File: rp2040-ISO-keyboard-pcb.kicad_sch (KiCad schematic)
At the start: 32 parts

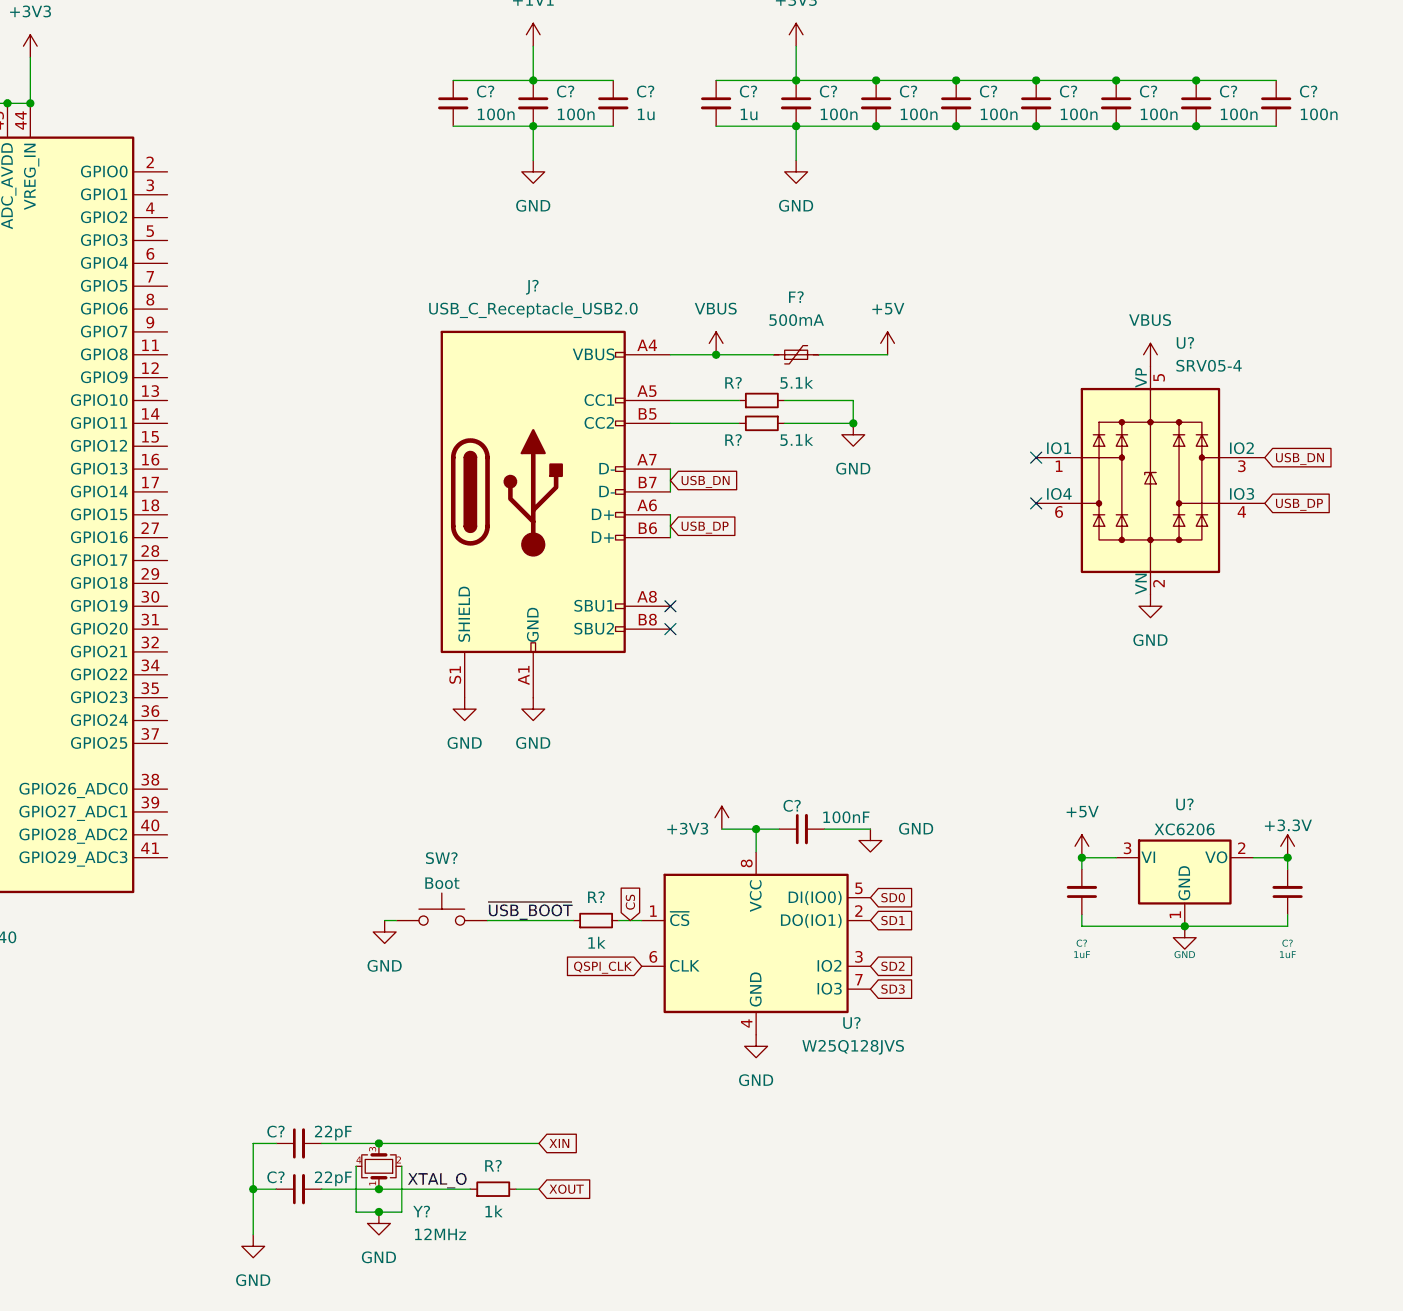
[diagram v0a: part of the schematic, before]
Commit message: added keymatrix with stabs
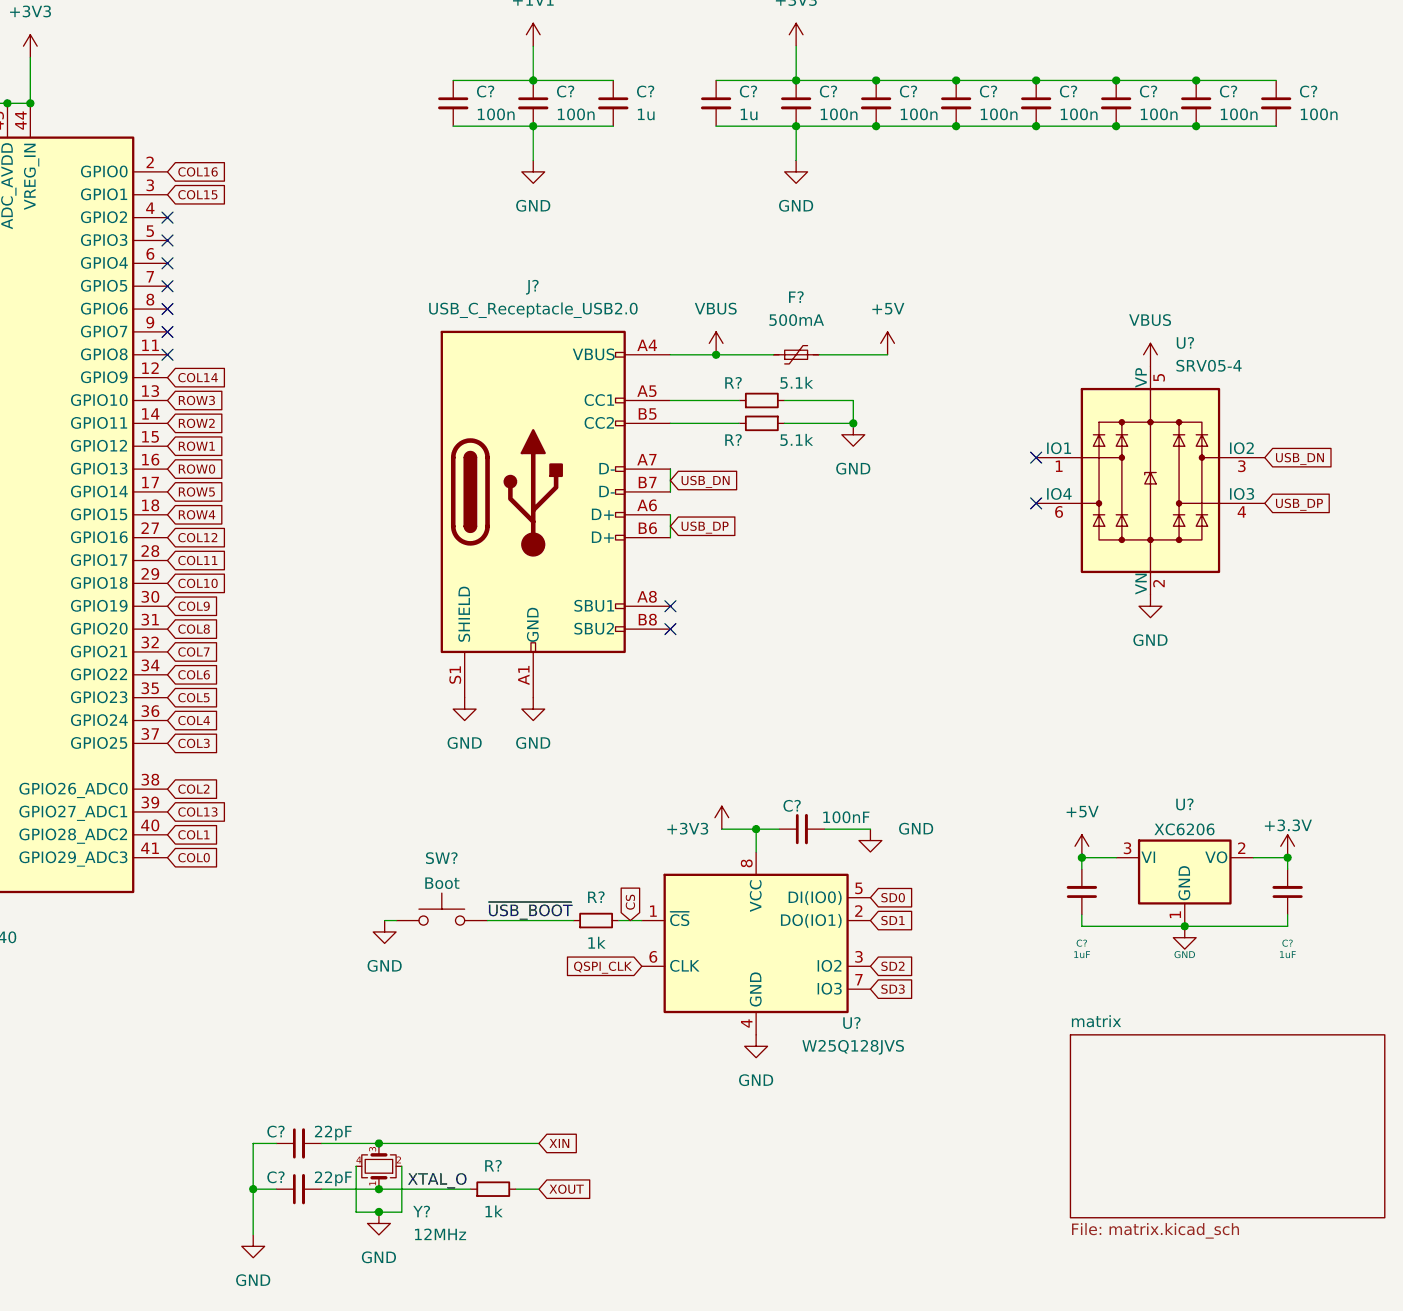
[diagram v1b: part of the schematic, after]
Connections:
- net COL14: now reaches U?.12 (GPIO9)
- net ROW3: now reaches U?.13 (GPIO10)
- net ROW2: now reaches U?.14 (GPIO11)
- net ROW1: now reaches U?.15 (GPIO12)
- net ROW0: now reaches U?.16 (GPIO13)
- net ROW5: now reaches U?.17 (GPIO14)
- net ROW4: now reaches U?.18 (GPIO15)
- net COL16: now reaches U?.2 (GPIO0)
- net COL12: now reaches U?.27 (GPIO16)
- net COL11: now reaches U?.28 (GPIO17)
- net COL10: now reaches U?.29 (GPIO18)
- net COL15: now reaches U?.3 (GPIO1)
- net COL9: now reaches U?.30 (GPIO19)
- net COL8: now reaches U?.31 (GPIO20)
- net COL7: now reaches U?.32 (GPIO21)
- net COL6: now reaches U?.34 (GPIO22)
- net COL5: now reaches U?.35 (GPIO23)
- net COL4: now reaches U?.36 (GPIO24)
- net COL3: now reaches U?.37 (GPIO25)
- net COL2: now reaches U?.38 (GPIO26_ADC0)
- net COL13: now reaches U?.39 (GPIO27_ADC1)
- net COL1: now reaches U?.40 (GPIO28_ADC2)
- net COL0: now reaches U?.41 (GPIO29_ADC3)
- no-connect marks 4 -> 11
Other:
- added sheet matrix (matrix.kicad_sch)

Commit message: added capacitors for LEDs and annotatios
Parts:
- added C94: 10uf, symbol Device:C_Small
- gave numbers to parts that had none: 32
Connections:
- net USB_DN is gone; now on net DN: J1.A7 (D-), J1.B7 (D-), U1.3 (IO2)
- net USB_DP is gone; now on net DP: J1.A6 (D+), J1.B6 (D+), U1.4 (IO3)
- net +3V3: now also C94.1
- net GND: now also C94.2
- net RGB: now reaches U2.4 (GPIO2)
- net CS renamed SS
- no-connect marks 11 -> 10
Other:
- added sheet led_capacitors (led_capacitors.kicad_sch)
- added sheet matrix_led (matix_led.kicad_sch)
- moved on the sheet: C100, C101, C102, C103, C104, C105, C106, C107, C95, C96, C97, C98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

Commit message: added footprints to compontents
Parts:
- C100, C101, C102, C91, C92, C93, C94, C95, C96, C97, C98, C99: footprint (none) -> Capacitor_SMD:C_0402_1005Metric
- F1: footprint (none) -> Fuse:Fuse_1206_3216Metric
- J1: footprint (none) -> Connector_USB:USB_C_Receptacle_HRO_TYPE-C-31-M-12
- R2, R3: footprint (none) -> Resistor_SMD:R_0603_1608Metric
- R4, R5: footprint (none) -> Resistor_SMD:R_0402_1005Metric

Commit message: loaded and fipped footprints to pcb editor
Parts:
- removed J2: SWD, Connector_PinSocket_2.54mm:PinSocket_1x05_P2.54mm_Vertical, symbol Connector_Generic:Conn_01x05
- added SW02: Boot, Connector_PinSocket_2.54mm:PinSocket_1x02_P2.54mm_Vertical, symbol Switch:SW_Push
- renumbered SW0 to SW01
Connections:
- net GND: now also SW02.1
- net SWCLK: no longer names the net of U2.24 (SWCLK)
- net SWD: no longer names the net of U2.25 (SWD)
- net ~{RESET}: no longer names the net of R1.2, U2.26 (RUN)
- net ~{RESET}: now also SW02.2
- no-connect marks 10 -> 12

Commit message: placed switches and LEDs
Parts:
- renumbered SW01 to btn1, SW02 to btn2

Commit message: IS313741A added with some wires
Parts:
- added C? (x4): 100nF, Capacitor_SMD:C_0402_1005Metric, symbol Device:C_Small
- added C? (x3): 1uF, Capacitor_SMD:C_0402_1005Metric, symbol Device:C_Small
- added R?: 100k, Resistor_SMD:R_0603_1608Metric, symbol Device:R_Small
- added R? (x2): 2k, Resistor_SMD:R_0603_1608Metric, symbol Device:R_Small
- added R?: 10k, Resistor_SMD:R_0603_1608Metric, symbol Device:R_Small
- added U?: IS313741A, marbastlib-various:QFN-60_EP_7x7_Pitch0.4mm, symbol marbastlib-various:IS313741A
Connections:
- net +3V3: now also C?.1, C?.1, C?.1, C?.1, C?.1, C?.1, R?.2, R?.2, U?.14 (AVCC), U?.15 (PVCC), U?.25 (PVCC)
- net GND: now also C?.2, C?.2, C?.2, C?.2, C?.2, C?.2, R?.1, U?.12 (GND), U?.36 (GND), U?.55 (GND), U?.61 (GND), U?.8 (ADDR)
- new net: C?.1, R?.1
- new net: R?.2, U?.13 (ISET)
- new net SCL: R?.1, U?.10 (SCL)
- new net SDA: R?.1, U?.9 (SDA)
- new net ~{SDB}: C?.2, R?.2, U?.11 (~{SDB})
- no-connect marks 12 -> 13

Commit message: added sw and cs labels to led driver
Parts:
- added R?: 100k, Capacitor_SMD:C_0402_1005Metric, symbol Device:R_Small
- added U?: SN74LV1T34DCKR, Package_TO_SOT_SMD:SOT-353_SC-70-5, symbol Bonsai_C4:SN74LV1T34DCKR
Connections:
- net +3V3: now also R?.1; no longer C?.1, C?.1, C?.1, C?.1, C?.1, C?.1, U?.14 (AVCC), U?.15 (PVCC), U?.25 (PVCC)
- net +5V: now also C?.1, C?.1, C?.1, C?.1, C?.1, C?.1, U?.14 (AVCC), U?.15 (PVCC), U?.25 (PVCC), U?.5 (VCC)
- net GND: now also U?.3 (GND)
- net RGB: now also R?.2, U?.2
- net CS34: now reaches U?.1 (CS34)
- net SW1: now reaches U?.16 (SW1)
- net SW2: now reaches U?.17 (SW2)
- net SW3: now reaches U?.18 (SW3)
- net SW4: now reaches U?.19 (SW4)
- net CS35: now reaches U?.2 (CS35)
- net SW5: now reaches U?.20 (SW5)
- net SW6: now reaches U?.21 (SW6)
- net SW7: now reaches U?.22 (SW7)
- net SW8: now reaches U?.23 (SW8)
- net SW9: now reaches U?.24 (SW9)
- net CS1: now reaches U?.26 (CS1)
- net CS2: now reaches U?.27 (CS2)
- net CS3: now reaches U?.28 (CS3)
- net CS4: now reaches U?.29 (CS4)
- net CS36: now reaches U?.3 (CS36)
- net CS5: now reaches U?.30 (CS5)
- net CS6: now reaches U?.31 (CS6)
- net CS7: now reaches U?.32 (CS7)
- net CS8: now reaches U?.33 (CS8)
- net CS9: now reaches U?.34 (CS9)
- net CS10: now reaches U?.35 (CS10)
- net CS11: now reaches U?.37 (CS11)
- net CS12: now reaches U?.38 (CS12)
- net CS13: now reaches U?.39 (CS13)
- net CS37: now reaches U?.4 (CS37)
- net CS14: now reaches U?.40 (CS14)
- net CS15: now reaches U?.41 (CS15)
- net CS16: now reaches U?.42 (CS16)
- net CS17: now reaches U?.43 (CS17)
- net CS18: now reaches U?.44 (CS15)
- net CS19: now reaches U?.45 (CS19)
- net CS20: now reaches U?.46 (CS20)
- net CS21: now reaches U?.47 (CS21)
- net CS22: now reaches U?.48 (CS22)
- net CS23: now reaches U?.49 (CS23)
- net CS38: now reaches U?.5 (CS38)
- net CS24: now reaches U?.50 (CS24)
- net CS25: now reaches U?.51 (CS25)
- net CS26: now reaches U?.52 (CS26)
- net CS27: now reaches U?.53 (CS27)
- net CS28: now reaches U?.54 (CS28)
- net CS29: now reaches U?.56 (CS29)
- net CS130: now reaches U?.57 (CS30)
- net CS31: now reaches U?.58 (CS31)
- net CS32: now reaches U?.59 (CS32)
- net CS39: now reaches U?.6 (CS39)
- net CS33: now reaches U?.60 (CS33)
- new net RGB_5V: U?.4
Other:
- removed sheet led_capacitors
- removed sheet matrix_led

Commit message: added rgb matrix
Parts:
- added R11, R16, R17, R19, R20, R22, R23, R25, R26, R28, R29, R31, R32, R34, R35, R38, R39, R41, R42, R44, R45, R48, R49, R6, R7, R9: 20k, Resistor_SMD:R_0603_1608Metric, symbol Device:R_Small
- added R14, R18, R21, R24, R27, R30, R33, R37, R40, R43, R47, R50, R8: 51k, Resistor_SMD:R_0603_1608Metric, symbol Device:R_Small
- gave numbers to parts that had none: 14
- renumbered C97 to C10, C98 to C11, C99 to C12, C100 to C13, C101 to C14, C102 to C15, C103 to C20, C104 to C21, C105 to C22, C106 to C23, C107 to C24, C91 to C4, C92 to C5, C93 to C6, C94 to C7, C95 to C8, C96 to C9, R4 to R12, R5 to R15, R6 to R36, R2 to R4, R7 to R46, R3 to R5, U3 to U4, U4 to U5, btn2 to btn1, btn1 to btn2
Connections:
- net CS1: now also R6.2; no longer U3.26 (CS1)
- net CS10: now also R19.2; no longer U3.35 (CS10)
- net CS11: now also R20.2; no longer U3.37 (CS11)
- net CS12: now also R21.2; no longer U3.38 (CS12)
- net CS13: now also R22.2; no longer U3.39 (CS13)
- net CS14: now also R23.2; no longer U3.40 (CS14)
- net CS15: now also R24.2; no longer U3.41 (CS15)
- net CS16: now also R25.2; no longer U3.42 (CS16)
- net CS17: now also R26.2; no longer U3.43 (CS17)
- net CS18: now also R27.2; no longer U3.44 (CS15)
- net CS19: now also R28.2; no longer U3.45 (CS19)
- net CS2: now also R7.2; no longer U3.27 (CS2)
- net CS20: now also R29.2; no longer U3.46 (CS20)
- net CS21: now also R30.2; no longer U3.47 (CS21)
- net CS22: now also R31.2; no longer U3.48 (CS22)
- net CS23: now also R32.2; no longer U3.49 (CS23)
- net CS24: now also R33.2; no longer U3.50 (CS24)
- net CS25: now also R34.2; no longer U3.51 (CS25)
- net CS26: now also R35.2; no longer U3.52 (CS26)
- net CS27: now also R37.2; no longer U3.53 (CS27)
- net CS28: now also R38.2; no longer U3.54 (CS28)
- net CS29: now also R39.2; no longer U3.56 (CS29)
- net CS3: now also R8.2; no longer U3.28 (CS3)
- net CS31: now also R41.2; no longer U3.58 (CS31)
- net CS32: now also R42.2; no longer U3.59 (CS32)
- net CS33: now also R43.2; no longer U3.60 (CS33)
- net CS34: now also R44.2; no longer U3.1 (CS34)
- net CS35: now also R45.2; no longer U3.2 (CS35)
- net CS36: now also R47.2; no longer U3.3 (CS36)
- net CS37: now also R48.2; no longer U3.4 (CS37)
- net CS38: now also R49.2; no longer U3.5 (CS38)
- net CS39: now also R50.2; no longer U3.6 (CS39)
- net CS4: now also R9.2; no longer U3.29 (CS4)
- net CS5: now also R11.2; no longer U3.30 (CS5)
- net CS6: now also R14.2; no longer U3.31 (CS6)
- net CS7: now also R16.2; no longer U3.32 (CS7)
- net CS8: now also R17.2; no longer U3.33 (CS8)
- net CS9: now also R18.2; no longer U3.34 (CS9)
- net CS130: no longer names the net of U3.57 (CS30)
- net CS130: now also R40.1
- new net: R26.1, U3.43 (CS17)
- new net: R32.1, U3.49 (CS23)
- new net: R20.1, U3.37 (CS11)
- new net: R47.1, U3.3 (CS36)
- new net: R14.1, U3.31 (CS6)
- new net: R48.1, U3.4 (CS37)
- new net: R31.1, U3.48 (CS22)
- new net: R21.1, U3.38 (CS12)
- new net: R9.1, U3.29 (CS4)
- new net: R25.1, U3.42 (CS16)
- new net: R29.1, U3.46 (CS20)
- new net: R33.1, U3.50 (CS24)
- new net: R22.1, U3.39 (CS13)
- new net: R37.1, U3.53 (CS27)
- new net: R17.1, U3.33 (CS8)
- new net: R41.1, U3.58 (CS31)
- new net: R8.1, U3.28 (CS3)
- new net: R50.1, U3.6 (CS39)
- new net: R24.1, U3.41 (CS15)
- new net: R35.1, U3.52 (CS26)
- new net: R23.1, U3.40 (CS14)
- new net: R38.1, U3.54 (CS28)
- new net: R30.1, U3.47 (CS21)
- new net: R43.1, U3.60 (CS33)
- new net: R16.1, U3.32 (CS7)
- new net: R49.1, U3.5 (CS38)
- new net: R7.1, U3.27 (CS2)
- new net: R6.1, U3.26 (CS1)
- new net: R18.1, U3.34 (CS9)
- new net: R44.1, U3.1 (CS34)
- new net: R42.1, U3.59 (CS32)
- new net: R27.1, U3.44 (CS15)
- new net: R39.1, U3.56 (CS29)
- new net: R28.1, U3.45 (CS19)
- new net: R19.1, U3.35 (CS10)
- new net: R45.1, U3.2 (CS35)
- new net: R34.1, U3.51 (CS25)
- new net: R11.1, U3.30 (CS5)
- new net CS30: R40.2
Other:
- added sheet RGB_matrix (RGB_matrix.kicad_sch)
